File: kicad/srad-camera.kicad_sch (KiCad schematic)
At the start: 16 parts, among them J1 DEBUG, SW1 POWER, SW2 USER, SW3 BOOT0

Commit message: Mark as R1.0
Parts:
- renumbered C127 to C1, FB3 to FB1, R3 to R1, R4 to R2, R5 to R3, R6 to R4, R7 to R5, R1 to R6, R2 to R7
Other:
- company: (none) -> UVic Rocketry
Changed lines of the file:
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@@
 	(title_block
 		(title "SRAD Camera")
+		(date "2025-11-23")
+		(rev "1.0")
+		(company "UVic Rocketry")
+		(comment 1 "Author: Eric Handley")
 	)
 	(bus_alias "MIPI_BUS"
@@
 		(on_board yes)
 		(dnp no)
-		(property "Reference" "FB3"
+		(property "Reference" "FB1"
 			(at 141.0081 165.1 90)
 			(effects
@@
 			(project ""
 				(path "/da62c771-e8c9-451f-8df1-ec995aadcb11"
-					(reference "FB3")
+					(reference "FB1")
 					(unit 1)
 				)
@@
 		(dnp no)
 		(fields_autoplaced yes)
-		(property "Reference" "#PWR08"
+		(property "Reference" "#PWR013"
 			(at 66.04 158.75 0)
 			(effects
@@
 			(project "srad-camera"
 				(path "/da62c771-e8c9-451f-8df1-ec995aadcb11"
-					(reference "#PWR08")
+					(reference "#PWR013")
 					(unit 1)
 				)
@@
 		(on_board yes)
 		(dnp no)
-		(property "Reference" "#PWR073"
+		(property "Reference" "#PWR014"
 			(at 71.12 158.75 0)
 			(effects
@@
 			(project "srad-camera"
 				(path "/da62c771-e8c9-451f-8df1-ec995aadcb11"
-					(reference "#PWR073")
+					(reference "#PWR014")
 					(unit 1)
 				)
@@
 		(on_board yes)
 		(dnp no)
-		(property "Reference" "#PWR012"
+		(property "Reference" "#PWR05"
 			(at 243.84 80.01 0)
 			(effects
@@
 			(project "srad-camera"
 				(path "/da62c771-e8c9-451f-8df1-ec995aadcb11"
-					(reference "#PWR012")
+					(reference "#PWR05")
 					(unit 1)
 				)
@@
 		(on_board yes)
 		(dnp no)
-		(property "Reference" "R4"
+		(property "Reference" "R2"
 			(at 212.344 73.914 0)
 			(effects
@@
 			(project "srad-camera"
 				(path "/da62c771-e8c9-451f-8df1-ec995aadcb11"
-					(reference "R4")
+					(reference "R2")
 					(unit 1)
 				)
@@
 		(on_board yes)
 		(dnp no)
-		(property "Reference" "#PWR010"
+		(property "Reference" "#PWR04"
 			(at 199.39 66.04 0)
 			(effects
@@
 			(project "srad-camera"
 				(path "/da62c771-e8c9-451f-8df1-ec995aadcb11"
-					(reference "#PWR010")
+					(reference "#PWR04")
 					(unit 1)
 				)
@@
 		(on_board yes)
 		(dnp no)
-		(property "Reference" "#PWR067"
+		(property "Reference" "#PWR017"
 			(at 160.02 179.07 0)
 			(effects
@@
 			(project "srad-camera"
 				(path "/da62c771-e8c9-451f-8df1-ec995aadcb11"
-					(reference "#PWR067")
+					(reference "#PWR017")
 					(unit 1)
 				)
@@
 		(on_board yes)
 		(dnp no)
-		(property "Reference" "C127"
+		(property "Reference" "C1"
 			(at 141.478 174.244 0)
 			(effects
@@
 			(project "srad-camera"
 				(path "/da62c771-e8c9-451f-8df1-ec995aadcb11"
-					(reference "C127")
+					(reference "C1")
 					(unit 1)
 				)
@@
 		(on_board yes)
 		(dnp no)
-		(property "Reference" "#PWR03"
+		(property "Reference" "#PWR011"
 			(at 66.04 115.57 0)
 			(effects
@@
 			(project "srad-camera"
 				(path "/da62c771-e8c9-451f-8df1-ec995aadcb11"
-					(reference "#PWR03")
+					(reference "#PWR011")
 					(unit 1)
 				)
@@
 		(on_board yes)
 		(dnp no)
-		(property "Reference" "R1"
+		(property "Reference" "R6"
 			(at 146.558 171.704 0)
 			(effects
@@
 			(project "srad-camera"
 				(path "/da62c771-e8c9-451f-8df1-ec995aadcb11"
-					(reference "R1")
+					(reference "R6")
 					(unit 1)
 				)
@@
 		(on_board yes)
 		(dnp no)
-		(property "Reference" "#PWR014"
+		(property "Reference" "#PWR06"
 			(at 187.96 96.52 0)
 			(effects
@@
 			(project "srad-camera"
 				(path "/da62c771-e8c9-451f-8df1-ec995aadcb11"
-					(reference "#PWR014")
+					(reference "#PWR06")
 					(unit 1)
 				)
@@
 		(on_board yes)
 		(dnp no)
-		(property "Reference" "#PWR04"
+		(property "Reference" "#PWR012"
 			(at 71.12 115.57 0)
 			(effects
@@
 			(project "srad-camera"
 				(path "/da62c771-e8c9-451f-8df1-ec995aadcb11"
-					(reference "#PWR04")
+					(reference "#PWR012")
 					(unit 1)
 				)
@@
 		(on_board yes)
 		(dnp no)
-		(property "Reference" "R7"
+		(property "Reference" "R5"
 			(at 204.47 85.598 90)
 			(effects
@@
 			(project "srad-camera"
 				(path "/da62c771-e8c9-451f-8df1-ec995aadcb11"
-					(reference "R7")
+					(reference "R5")
 					(unit 1)
 				)
@@
 		(on_board yes)
 		(dnp no)
-		(property "Reference" "R6"
+		(property "Reference" "R4"
 			(at 208.026 80.264 90)
 			(effects
@@
 			(project "srad-camera"
 				(path "/da62c771-e8c9-451f-8df1-ec995aadcb11"
-					(reference "R6")
+					(reference "R4")
 					(unit 1)
 				)
@@
 		(on_board yes)
 		(dnp no)
-		(property "Reference" "#PWR06"
+		(property "Reference" "#PWR02"
 			(at 102.87 53.34 0)
 			(effects
@@
 			(project "srad-camera"
 				(path "/da62c771-e8c9-451f-8df1-ec995aadcb11"
-					(reference "#PWR06")
+					(reference "#PWR02")
 					(unit 1)
 				)
@@
 		(on_board yes)
 		(dnp no)
-		(property "Reference" "#PWR02"
+		(property "Reference" "#PWR010"
 			(at 34.29 115.57 0)
 			(effects
@@
 			(project "srad-camera"
 				(path "/da62c771-e8c9-451f-8df1-ec995aadcb11"
-					(reference "#PWR02")
+					(reference "#PWR010")
 					(unit 1)
 				)
@@
 		(on_board yes)
 		(dnp no)
-		(property "Reference" "R2"
+		(property "Reference" "R7"
 			(at 150.622 171.704 0)
 			(effects
@@
 			(project "srad-camera"
 				(path "/da62c771-e8c9-451f-8df1-ec995aadcb11"
-					(reference "R2")
+					(reference "R7")
 					(unit 1)
 				)
@@
 		(on_board yes)
 		(dnp no)
-		(property "Reference" "#PWR07"
+		(property "Reference" "#PWR03"
 			(at 102.87 60.96 0)
 			(effects
@@
 			(project "srad-camera"
 				(path "/da62c771-e8c9-451f-8df1-ec995aadcb11"
-					(reference "#PWR07")
+					(reference "#PWR03")
 					(unit 1)
 				)
@@
 		(on_board yes)
 		(dnp no)
-		(property "Reference" "R3"
+		(property "Reference" "R1"
 			(at 204.216 73.914 0)
 			(effects
@@
 			(project "srad-camera"
 				(path "/da62c771-e8c9-451f-8df1-ec995aadcb11"
-					(reference "R3")
+					(reference "R1")
 					(unit 1)
 				)
@@
 		(on_board yes)
 		(dnp no)
-		(property "Reference" "#PWR09"
+		(property "Reference" "#PWR015"
 			(at 97.79 170.18 0)
 			(effects
@@
 			(project "srad-camera"
 				(path "/da62c771-e8c9-451f-8df1-ec995aadcb11"
-					(reference "#PWR09")
+					(reference "#PWR015")
 					(unit 1)
 				)
@@
 		(on_board yes)
 		(dnp no)
-		(property "Reference" "#PWR011"
+		(property "Reference" "#PWR016"
 			(at 142.24 170.18 0)
 			(effects
@@
 			(project "srad-camera"
 				(path "/da62c771-e8c9-451f-8df1-ec995aadcb11"
-					(reference "#PWR011")
+					(reference "#PWR016")
 					(unit 1)
 				)
@@
 		(on_board yes)
 		(dnp no)
-		(property "Reference" "#PWR015"
+		(property "Reference" "#PWR07"
 			(at 255.27 104.14 0)
 			(effects
@@
 			(project "srad-camera"
 				(path "/da62c771-e8c9-451f-8df1-ec995aadcb11"
-					(reference "#PWR015")
+					(reference "#PWR07")
 					(unit 1)
 				)
@@
 		(on_board yes)
 		(dnp no)
-		(property "Reference" "#PWR05"
+		(property "Reference" "#PWR01"
 			(at 76.2 53.34 0)
 			(effects
@@
 			(project "srad-camera"
 				(path "/da62c771-e8c9-451f-8df1-ec995aadcb11"
-					(reference "#PWR05")
+					(reference "#PWR01")
 					(unit 1)
 				)
@@
 		(on_board yes)
 		(dnp no)
-		(property "Reference" "#PWR016"
+		(property "Reference" "#PWR09"
 			(at 255.27 106.68 0)
 			(effects
@@
 			(project "srad-camera"
 				(path "/da62c771-e8c9-451f-8df1-ec995aadcb11"
-					(reference "#PWR016")
+					(reference "#PWR09")
 					(unit 1)
 				)
@@
 		(on_board yes)
 		(dnp no)
-		(property "Reference" "#PWR013"
+		(property "Reference" "#PWR018"
 			(at 143.51 184.15 0)
 			(effects
@@
 			(project ""
 				(path "/da62c771-e8c9-451f-8df1-ec995aadcb11"
-					(reference "#PWR013")
+					(reference "#PWR018")
 					(unit 1)
 				)
@@
 		(on_board yes)
 		(dnp no)
-		(property "Reference" "#PWR01"
+		(property "Reference" "#PWR08"
 			(at 96.52 106.68 0)
 			(effects
@@
 			(project "srad-camera"
 				(path "/da62c771-e8c9-451f-8df1-ec995aadcb11"
-					(reference "#PWR01")
+					(reference "#PWR08")
 					(unit 1)
 				)
@@
 		(on_board yes)
 		(dnp no)
-		(property "Reference" "R5"
+		(property "Reference" "R3"
 			(at 238.506 73.914 0)
 			(effects
@@
 			(project "srad-camera"
 				(path "/da62c771-e8c9-451f-8df1-ec995aadcb11"
-					(reference "R5")
+					(reference "R3")
 					(unit 1)
 				)

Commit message: Start on PCB design
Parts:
- C1: footprint (none) -> Capacitor_SMD:C_0603_1608Metric; LCSC PART NAME (none) -> C15849
- FB1: footprint (none) -> Resistor_SMD:R_0201_0603Metric; LCSC PART NAME (none) -> C14709
- FPC1: LCSC PART NAME 间距:0.5mm P数:22P 抽屉式 下接 -> (none)
- J1: footprint (none) -> Connector_PinHeader_1.27mm:PinHeader_2x05_P1.27mm_Vertical_SMD
- JST1: footprint (none) -> Connector_JST:JST_XH_B3B-XH-A_1x03_P2.50mm_Vertical
- JST2: footprint (none) -> Connector_JST:JST_XH_B2B-XH-A_1x02_P2.50mm_Vertical
- R1, R2, R3: footprint (none) -> Resistor_SMD:R_0402_1005Metric; LCSC PART NAME (none) -> C25744
- R4, R5: value 47 -> 22R; footprint (none) -> Resistor_SMD:R_0402_1005Metric; LCSC PART NAME (none) -> C25092
- R6, R7: value 2.2k -> 4.7k; footprint (none) -> Resistor_SMD:R_0402_1005Metric; LCSC PART NAME (none) -> C25900
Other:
- sheet RK3566 SoC ports: added USB_OTG_DN, USB_OTG_DP; removed USB_DM, USB_DP
- sheet USBC 2.0 OTG ports: added USB_DN; removed USB_DM
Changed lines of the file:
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@@
 		)
 	)
-	(label "USB_DM"
+	(label "USB_DN"
 		(at 132.08 125.73 180)
 		(effects
@@
 		)
 	)
-	(label "USB_DM"
+	(label "USB_DN"
 		(at 110.49 45.72 180)
 		(effects
@@
 			)
 		)
-		(property "Footprint" ""
+		(property "Footprint" "Resistor_SMD:R_0201_0603Metric"
 			(at 140.97 171.958 90)
 			(effects
@@
 			)
 		)
+		(property "LCSC PART NAME" "C14709"
+			(at 140.97 170.18 90)
+			(effects
+				(font
+					(size 1.27 1.27)
+				)
+				(hide yes)
+			)
+		)
 		(pin "2"
 		)
@@
 			)
 		)
-		(property "Footprint" ""
+		(property "Footprint" "Connector_JST:JST_XH_B3B-XH-A_1x03_P2.50mm_Vertical"
 			(at 67.31 48.26 0)
 			(effects
@@
 			)
 		)
-		(property "Footprint" ""
+		(property "Footprint" "Resistor_SMD:R_0402_1005Metric"
 			(at 215.9 74.93 0)
 			(effects
@@
 			)
 		)
+		(property "LCSC PART NAME" "C25744"
+			(at 215.9 74.93 0)
+			(effects
+				(font
+					(size 1.27 1.27)
+				)
+				(hide yes)
+			)
+		)
 		(pin "2"
 		)
@@
 			)
 		)
-		(property "Footprint" ""
+		(property "Footprint" "Capacitor_SMD:C_0603_1608Metric"
 			(at 143.51 173.99 0)
 			(effects
@@
 			)
 		)
-		(property "V" ""
-			(at 143.51 173.99 90)
+		(property "LCSC PART NAME" "C15849"
+			(at 143.51 173.99 0)
 			(effects
 				(font
@@
 			)
 		)
-		(property "Value" "2.2k"
+		(property "Value" "4.7k"
 			(at 148.59 173.736 0)
 			(effects
@@
 			)
 		)
-		(property "Footprint" ""
+		(property "Footprint" "Resistor_SMD:R_0402_1005Metric"
 			(at 147.32 166.37 0)
 			(effects
@@
 			)
 		)
+		(property "LCSC PART NAME" "C25900"
+			(at 147.32 166.37 0)
+			(effects
+				(font
+					(size 1.27 1.27)
+				)
+				(hide yes)
+			)
+		)
 		(pin "1"
 		)
@@
 			)
 		)
-		(property "LCSC PART NAME" "间距:0.5mm P数:22P 抽屉式 下接"
+		(property "LCSC PART NAME" ""
 			(at 160.02 138.43 0)
 			(effects
@@
 			)
 		)
-		(property "Value" "47"
+		(property "Value" "22R"
 			(at 204.47 87.63 90)
 			(effects
@@
 			)
 		)
-		(property "Footprint" ""
+		(property "Footprint" "Resistor_SMD:R_0402_1005Metric"
 			(at 204.47 83.82 0)
 			(effects
@@
 			)
 		)
+		(property "LCSC PART NAME" "C25092"
+			(at 204.47 83.82 90)
+			(effects
+				(font
+					(size 1.27 1.27)
+				)
+				(hide yes)
+			)
+		)
 		(pin "2"
 		)
@@
 			)
 		)
-		(property "Value" "47"
+		(property "Value" "22R"
 			(at 208.026 82.296 90)
 			(effects
@@
 			)
 		)
-		(property "Footprint" ""
+		(property "Footprint" "Resistor_SMD:R_0402_1005Metric"
 			(at 204.47 81.28 0)
 			(effects
@@
 			)
 		)
+		(property "LCSC PART NAME" "C25092"
+			(at 204.47 81.28 90)
+			(effects
+				(font
+					(size 1.27 1.27)
+				)
+				(hide yes)
+			)
+		)
 		(pin "2"
 		)
@@
 			)
 		)
-		(property "Value" "2.2k"
+		(property "Value" "4.7k"
 			(at 149.86 172.974 90)
 			(effects
@@
 			)
 		)
-		(property "Footprint" ""
+		(property "Footprint" "Resistor_SMD:R_0402_1005Metric"
 			(at 149.86 166.37 0)
 			(effects
@@
 			)
 		)
+		(property "LCSC PART NAME" "C25900"
+			(at 149.86 166.37 0)
+			(effects
+				(font
+					(size 1.27 1.27)
+				)
+				(hide yes)
+			)
+		)
 		(pin "1"
 		)
@@
 			)
 		)
-		(property "Footprint" ""
+		(property "Footprint" "Resistor_SMD:R_0402_1005Metric"
 			(at 200.66 74.93 0)
 			(effects
@@
 			)
 		)
+		(property "LCSC PART NAME" "C25744"
+			(at 200.66 74.93 0)
+			(effects
+				(font
+					(size 1.27 1.27)
+				)
+				(hide yes)
+			)
+		)
 		(pin "2"
 		)
@@
 			)
 		)
-		(property "Footprint" ""
+		(property "Footprint" "Connector_JST:JST_XH_B2B-XH-A_1x02_P2.50mm_Vertical"
 			(at 196.85 107.95 0)
 			(effects
@@
 			)
 		)
-		(property "Footprint" ""
+		(property "Footprint" "Connector_PinHeader_1.27mm:PinHeader_2x05_P1.27mm_Vertical_SMD"
 			(at 193.04 86.36 0)
 			(effects
@@
 			)
 		)
-		(property "Footprint" ""
+		(property "Footprint" "Resistor_SMD:R_0402_1005Metric"
 			(at 234.95 74.93 0)
 			(effects
@@
 			)
 		)
+		(property "LCSC PART NAME" "C25744"
+			(at 234.95 74.93 0)
+			(effects
+				(font
+					(size 1.27 1.27)
+				)
+				(hide yes)
+			)
+		)
 		(pin "2"
 		)
@@
 			)
 		)
-		(pin "USB_DM" input
+		(pin "USB_OTG_DN" input
 			(at 115.57 125.73 0)
 			(effects
@@
 			)
 		)
-		(pin "USB_DP" input
+		(pin "USB_OTG_DP" input
 			(at 115.57 128.27 0)
 			(effects
@@
 			)
 		)
-		(pin "USB_DM" output
+		(pin "USB_DN" output
 			(at 100.33 45.72 0)
 			(effects

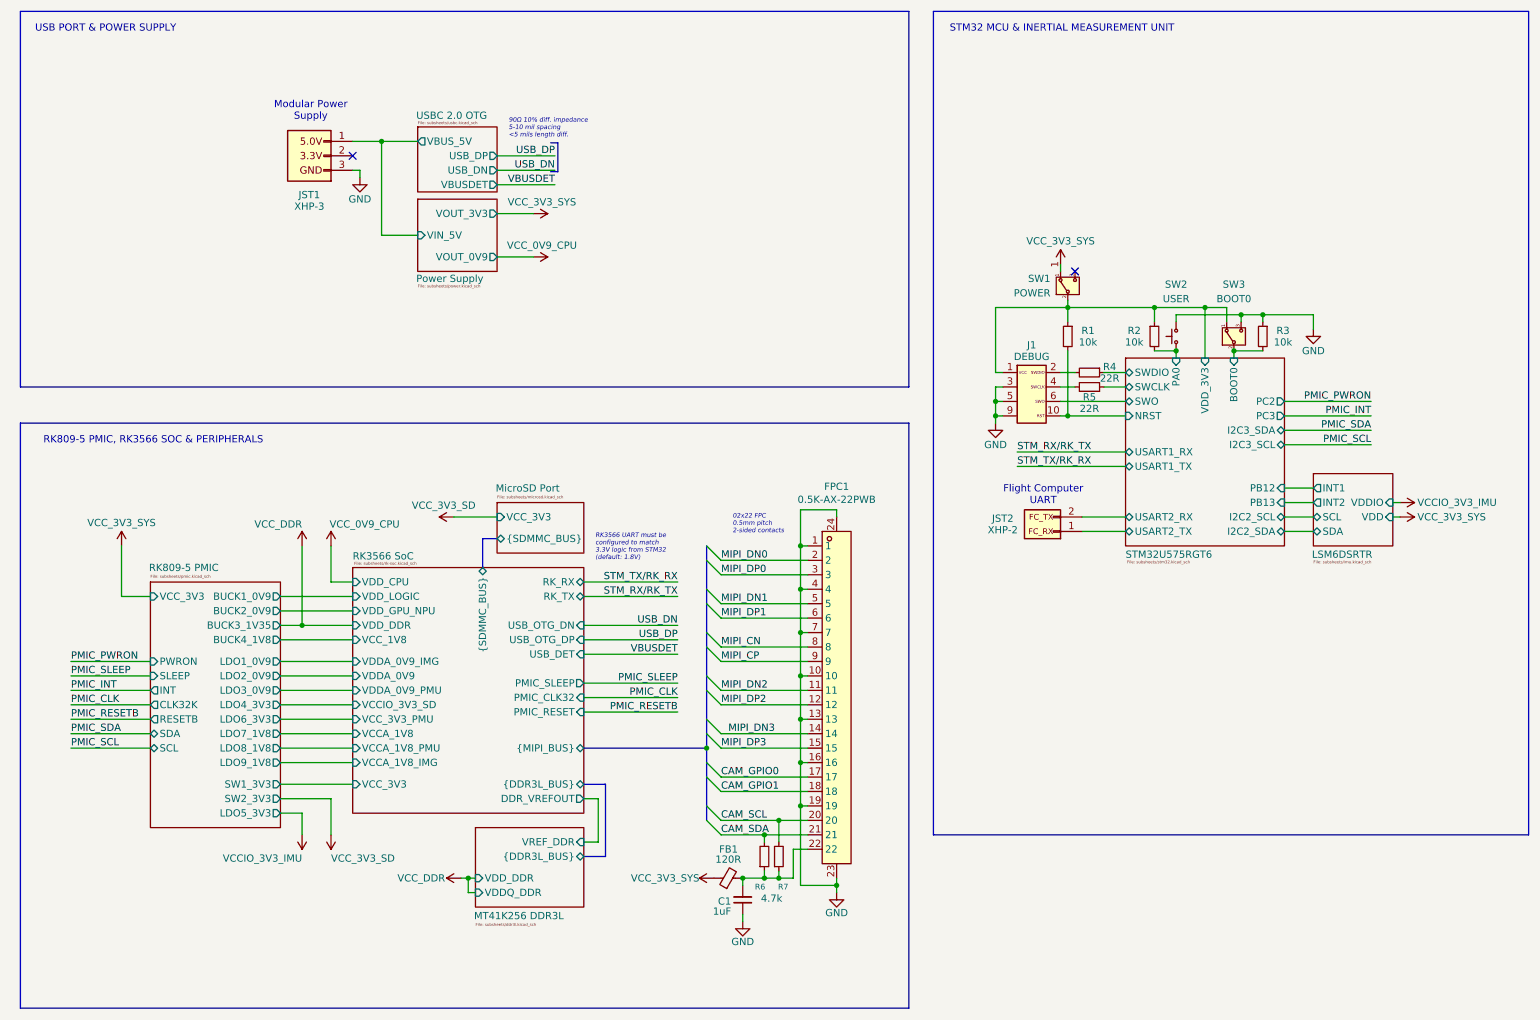
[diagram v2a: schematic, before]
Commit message: Remove power/decoupling for unused power domains
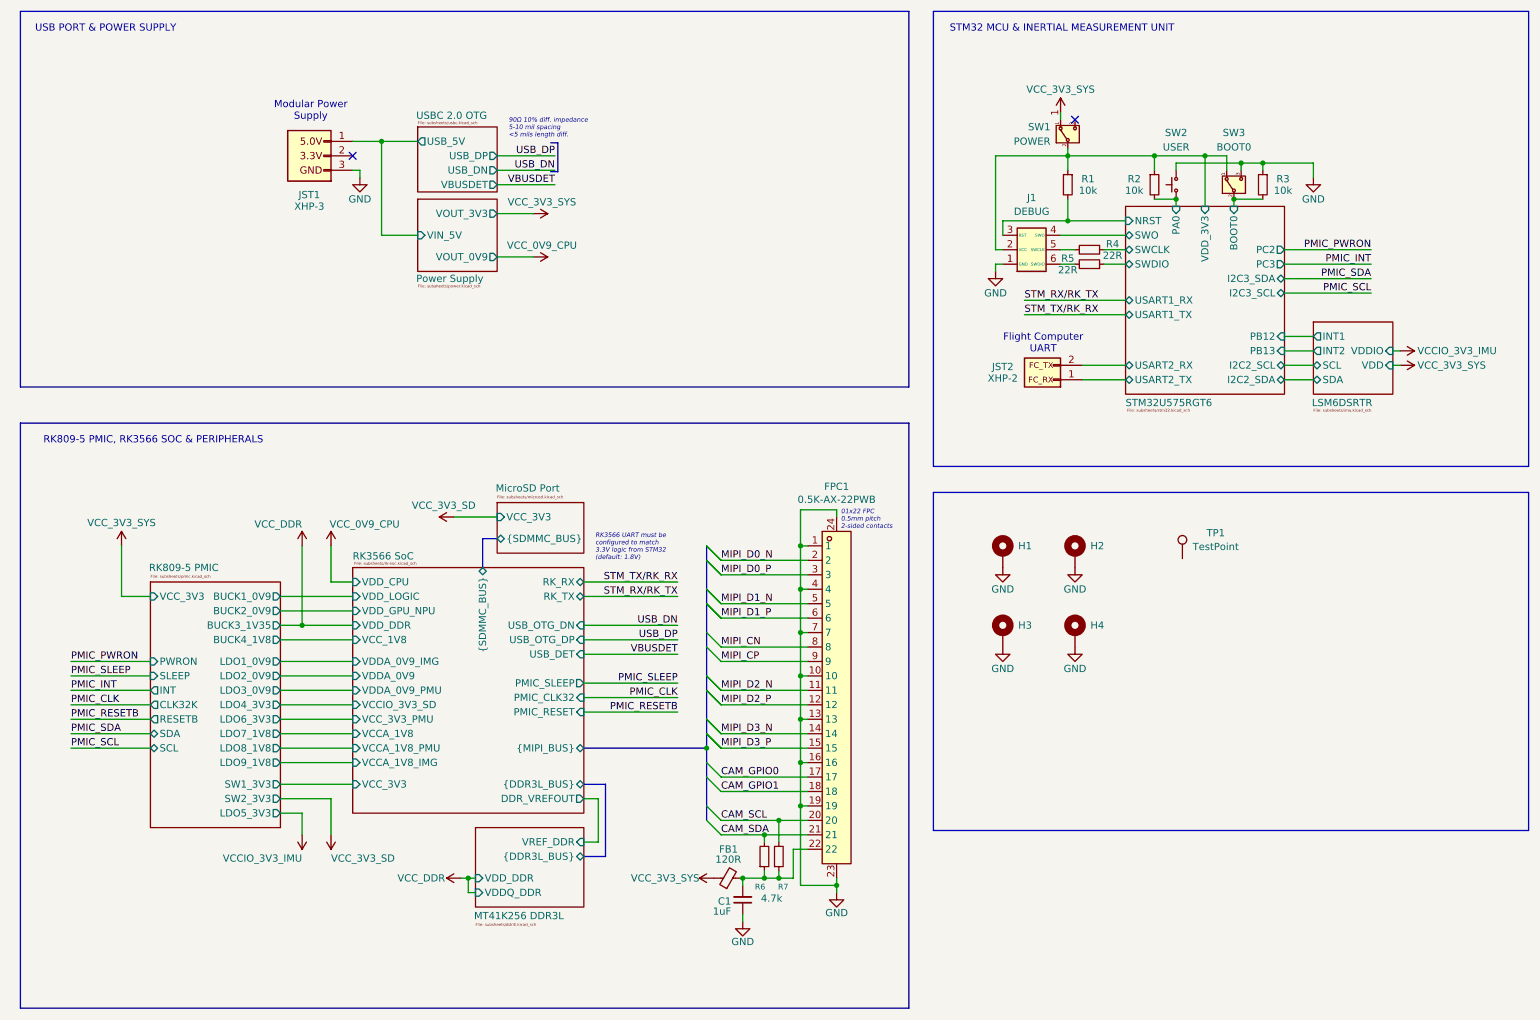
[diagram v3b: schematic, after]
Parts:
- removed J1: DEBUG, Connector_PinHeader_1.27mm:PinHeader_2x05_P1.27mm_Vertical_SMD, symbol Connector_Generic:Conn_02x05_Odd_Even
- added H1, H2, H3, H4: MntHole, srad-camera-footprints:4-40_MountingHole, symbol Mechanical:MountingHole_Pad_MP
- added J1: DEBUG, Connector_PinHeader_1.27mm:PinHeader_2x03_P1.27mm_Vertical, symbol Connector_Generic:Conn_02x03_Counter_Clockwise
- added TP1: TestPoint, symbol Connector:TestPoint
- SW1, SW3: footprint (none) -> Button_Switch_SMD:SW_SPDT_PCM12
- SW2: footprint (none) -> Button_Switch_SMD:SW_SPST_EVQP2_MiddlePushTravel_H2.5mm
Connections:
- net GND: now also H1.1 (MP), H2.1 (MP), H3.1 (MP), H4.1 (MP), J1.1 (GND)
- net STM32U575RGT6/NRST: now also J1.3 (RST)
- net STM32U575RGT6/SWCLK: now also R4.1; no longer R5.1
- net STM32U575RGT6/SWDIO: now also R5.1; no longer R4.1
- net STM32U575RGT6/SWO: now also J1.4 (SWO)
- net STM32U575RGT6/VDD_3V3: now also J1.2 (VCC)
- net at R5.2: now also J1.6 (SWDIO)
- net at R4.2: now also J1.5 (SWCLK)
- net MIPI_DN0 renamed MIPI_D0_N
- net MIPI_DN1 renamed MIPI_D1_N
- net MIPI_DN2 renamed MIPI_D2_N
- net MIPI_DN3 renamed MIPI_D3_N
- net MIPI_DP0 renamed MIPI_D0_P
- net MIPI_DP1 renamed MIPI_D1_P
- net MIPI_DP2 renamed MIPI_D2_P
- net MIPI_DP3 renamed MIPI_D3_P
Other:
- sheet USBC 2.0 OTG ports: added USB_5V; removed VBUS_5V
- note added: "01x22 FPC 0.5mm pitch 2-sided contacts"
- note removed: "02x22 FPC 0.5mm pitch 2-sided contacts"
- moved on the sheet: JST2, R1, R2, R3, R4, R5, SW1, SW2, SW3
